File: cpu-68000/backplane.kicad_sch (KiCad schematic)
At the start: 12 parts, among them J201 Conn_03x32_Row_Letter_First

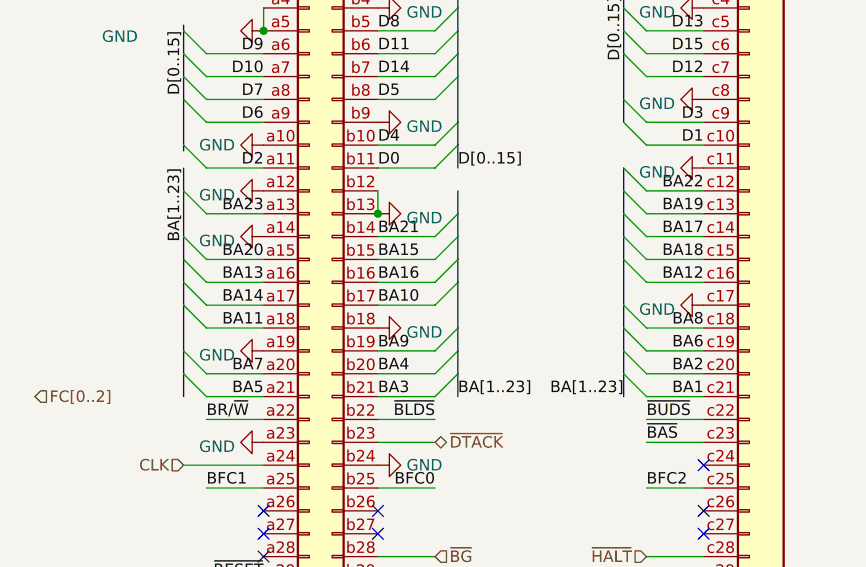
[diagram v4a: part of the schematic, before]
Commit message: Finished routing new address/data from backplane
- Routed the traces for the address/data bus from the connector and
  along the memories that need them. The NVRAM is fully connected to the
  bus, along with the peripheral section.

  We'll need to assign address lines to the SRAMs, then connect the
  flash chips next.
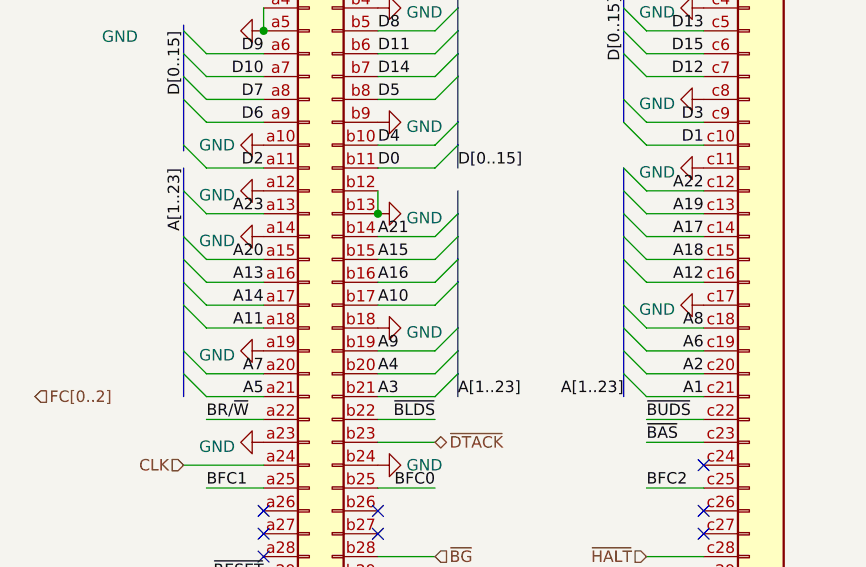
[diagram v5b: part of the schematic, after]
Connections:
- net A1: now also J201.c21 (Pin_c21)
- net A10: now also J201.b17 (Pin_b17)
- net A11: now also J201.a18 (Pin_a18)
- net A12: now also J201.c16 (Pin_c16)
- net A13: now also J201.a16 (Pin_a16)
- net A14: now also J201.a17 (Pin_a17)
- net A15: now also J201.b15 (Pin_b15)
- net A16: now also J201.b16 (Pin_b16)
- net A17: now also J201.c14 (Pin_c14)
- net A18: now also J201.c15 (Pin_c15)
- net A19: now also J201.c13 (Pin_c13)
- net A2: now also J201.c20 (Pin_c20)
- net A20: now also J201.a15 (Pin_a15)
- net A21: now also J201.b14 (Pin_b14)
- net A22: now also J201.c12 (Pin_c12)
- net A23: now also J201.a13 (Pin_a13)
- net A3: now also J201.b21 (Pin_b21)
- net A4: now also J201.b20 (Pin_b20)
- net A5: now also J201.a21 (Pin_a21)
- net A6: now also J201.c19 (Pin_c19)
- net A7: now also J201.a20 (Pin_a20)
- net A8: now also J201.c18 (Pin_c18)
- net A9: now also J201.b19 (Pin_b19)
- net BA1: no longer J201.c21 (Pin_c21)
- net BA10: no longer J201.b17 (Pin_b17)
- net BA11: no longer J201.a18 (Pin_a18)
- net BA12: no longer J201.c16 (Pin_c16)
- net BA13: no longer J201.a16 (Pin_a16)
- net BA14: no longer J201.a17 (Pin_a17)
- net BA15: no longer J201.b15 (Pin_b15)
- net BA16: no longer J201.b16 (Pin_b16)
- net BA17: no longer J201.c14 (Pin_c14)
- net BA18: no longer J201.c15 (Pin_c15)
- net BA19: no longer J201.c13 (Pin_c13)
- net BA2: no longer J201.c20 (Pin_c20)
- net BA20: no longer J201.a15 (Pin_a15)
- net BA21: no longer J201.b14 (Pin_b14)
- net BA22: no longer J201.c12 (Pin_c12)
- net BA23: no longer J201.a13 (Pin_a13)
- net BA3: no longer J201.b21 (Pin_b21)
- net BA4: no longer J201.b20 (Pin_b20)
- net BA5: no longer J201.a21 (Pin_a21)
- net BA6: no longer J201.c19 (Pin_c19)
- net BA7: no longer J201.a20 (Pin_a20)
- net BA8: no longer J201.c18 (Pin_c18)
- net BA9: no longer J201.b19 (Pin_b19)
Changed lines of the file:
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@@
     (effects (font (size 1.27 1.27)) (justify right bottom))
   )
-  (label "BA18" (at 264.16 54.61 180)
+  (label "A18" (at 264.16 54.61 180)
     (effects (font (size 1.27 1.27)) (justify right bottom))
   )
@@
     (effects (font (size 1.27 1.27)) (justify right bottom))
   )
-  (label "BA5" (at 215.265 69.85 180)
+  (label "A5" (at 215.265 69.85 180)
     (effects (font (size 1.27 1.27)) (justify right bottom))
   )
@@
     (effects (font (size 1.27 1.27)) (justify right bottom))
   )
-  (label "BA20" (at 215.265 54.61 180)
-    (effects (font (size 1.27 1.27)) (justify right bottom))
-  )
-  (label "BA2" (at 264.16 67.31 180)
-    (effects (font (size 1.27 1.27)) (justify right bottom))
-  )
-  (label "BA10" (at 227.965 59.69 0)
+  (label "A20" (at 215.265 54.61 180)
+    (effects (font (size 1.27 1.27)) (justify right bottom))
+  )
+  (label "A2" (at 264.16 67.31 180)
+    (effects (font (size 1.27 1.27)) (justify right bottom))
+  )
+  (label "A10" (at 227.965 59.69 0)
     (effects (font (size 1.27 1.27)) (justify left bottom))
   )
@@
     (effects (font (size 1.27 1.27)) (justify left bottom))
   )
-  (label "BA3" (at 227.965 69.85 0)
+  (label "A3" (at 227.965 69.85 0)
     (effects (font (size 1.27 1.27)) (justify left bottom))
   )
@@
     (effects (font (size 1.27 1.27)) (justify right bottom))
   )
-  (label "BA[1..23]" (at 255.27 69.85 180)
+  (label "A[1..23]" (at 255.27 69.85 180)
     (effects (font (size 1.27 1.27)) (justify right bottom))
   )
@@
     (effects (font (size 1.27 1.27)) (justify right bottom))
   )
-  (label "BA21" (at 227.965 52.07 0)
+  (label "A21" (at 227.965 52.07 0)
     (effects (font (size 1.27 1.27)) (justify left bottom))
   )
@@
     (effects (font (size 1.27 1.27)) (justify left bottom))
   )
-  (label "BA4" (at 227.965 67.31 0)
+  (label "A4" (at 227.965 67.31 0)
     (effects (font (size 1.27 1.27)) (justify left bottom))
   )
@@
     (effects (font (size 1.27 1.27)) (justify right bottom))
   )
-  (label "BA19" (at 264.16 49.53 180)
+  (label "A19" (at 264.16 49.53 180)
     (effects (font (size 1.27 1.27)) (justify right bottom))
   )
@@
     (effects (font (size 1.27 1.27)) (justify right bottom))
   )
-  (label "BA[1..23]" (at 236.855 69.85 0)
+  (label "A[1..23]" (at 236.855 69.85 0)
     (effects (font (size 1.27 1.27)) (justify left bottom))
   )
@@
     (effects (font (size 1.27 1.27)) (justify right bottom))
   )
-  (label "BA12" (at 264.16 57.15 180)
-    (effects (font (size 1.27 1.27)) (justify right bottom))
-  )
-  (label "BA14" (at 215.265 59.69 180)
+  (label "A12" (at 264.16 57.15 180)
+    (effects (font (size 1.27 1.27)) (justify right bottom))
+  )
+  (label "A14" (at 215.265 59.69 180)
     (effects (font (size 1.27 1.27)) (justify right bottom))
   )
@@
     (effects (font (size 1.27 1.27)) (justify right bottom))
   )
-  (label "BA7" (at 215.265 67.31 180)
+  (label "A7" (at 215.265 67.31 180)
     (effects (font (size 1.27 1.27)) (justify right bottom))
   )
@@
     (effects (font (size 1.27 1.27)) (justify left bottom))
   )
-  (label "BA11" (at 215.265 62.23 180)
+  (label "A11" (at 215.265 62.23 180)
     (effects (font (size 1.27 1.27)) (justify right bottom))
   )
@@
     (effects (font (size 1.27 1.27)) (justify left bottom))
   )
-  (label "BA17" (at 264.16 52.07 180)
+  (label "A17" (at 264.16 52.07 180)
     (effects (font (size 1.27 1.27)) (justify right bottom))
   )
@@
     (effects (font (size 1.27 1.27)) (justify left bottom))
   )
-  (label "BA15" (at 227.965 54.61 0)
+  (label "A15" (at 227.965 54.61 0)
     (effects (font (size 1.27 1.27)) (justify left bottom))
   )
@@
     (effects (font (size 1.27 1.27)) (justify right bottom))
   )
-  (label "BA8" (at 264.16 62.23 180)
+  (label "A8" (at 264.16 62.23 180)
     (effects (font (size 1.27 1.27)) (justify right bottom))
   )
@@
     (effects (font (size 1.27 1.27)) (justify right bottom))
   )
-  (label "BA23" (at 215.265 49.53 180)
+  (label "A23" (at 215.265 49.53 180)
     (effects (font (size 1.27 1.27)) (justify right bottom))
   )
@@
     (effects (font (size 1.27 1.27)) (justify right bottom))
   )
-  (label "BA22" (at 264.16 46.99 180)
+  (label "A22" (at 264.16 46.99 180)
     (effects (font (size 1.27 1.27)) (justify right bottom))
   )
@@
     (effects (font (size 1.27 1.27)) (justify left bottom))
   )
-  (label "BA1" (at 264.16 69.85 180)
-    (effects (font (size 1.27 1.27)) (justify right bottom))
-  )
-  (label "BA[1..23]" (at 206.375 44.45 270)
+  (label "A1" (at 264.16 69.85 180)
+    (effects (font (size 1.27 1.27)) (justify right bottom))
+  )
+  (label "A[1..23]" (at 206.375 44.45 270)
     (effects (font (size 1.27 1.27)) (justify right bottom))
   )
@@
     (effects (font (size 1.27 1.27)) (justify left bottom))
   )
-  (label "BA13" (at 215.265 57.15 180)
+  (label "A13" (at 215.265 57.15 180)
     (effects (font (size 1.27 1.27)) (justify right bottom))
   )
@@
     (effects (font (size 1.27 1.27)) (justify left bottom))
   )
-  (label "BA9" (at 227.965 64.77 0)
-    (effects (font (size 1.27 1.27)) (justify left bottom))
-  )
-  (label "BA6" (at 264.16 64.77 180)
+  (label "A9" (at 227.965 64.77 0)
+    (effects (font (size 1.27 1.27)) (justify left bottom))
+  )
+  (label "A6" (at 264.16 64.77 180)
     (effects (font (size 1.27 1.27)) (justify right bottom))
   )
@@
     (effects (font (size 1.27 1.27)) (justify right bottom))
   )
-  (label "BA16" (at 227.965 57.15 0)
-    (effects (font (size 1.27 1.27)) (justify left bottom))
-  )
+  (label "A16" (at 227.965 57.15 0)
+    (effects (font (size 1.27 1.27)) (justify left bottom))
+  )

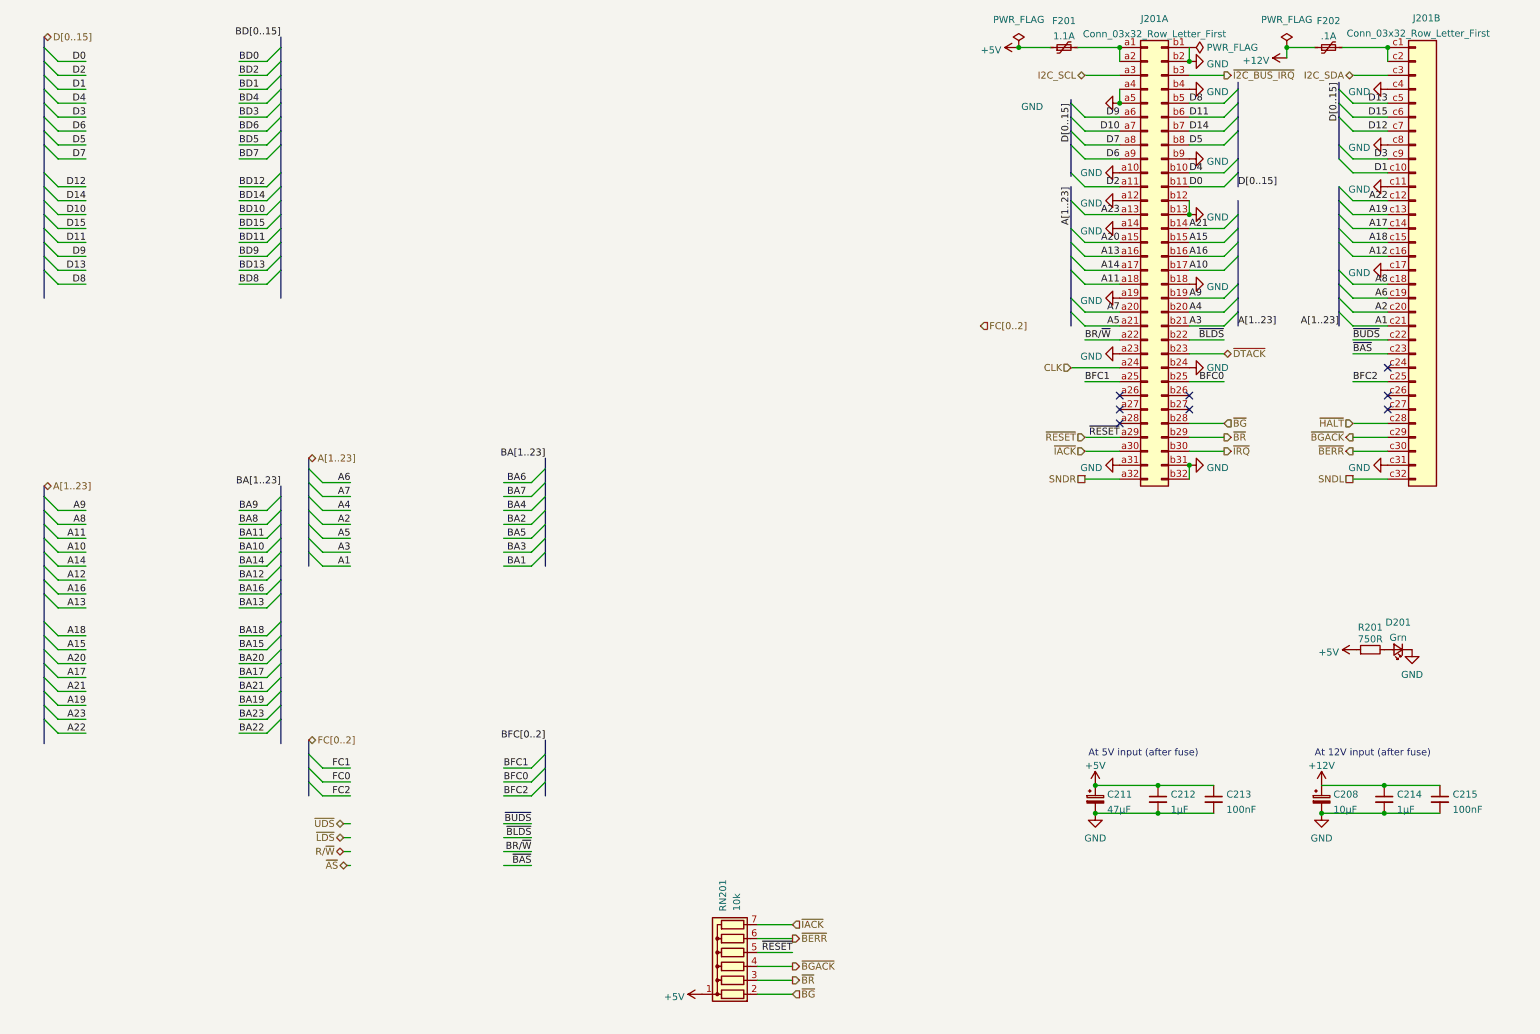
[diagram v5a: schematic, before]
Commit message: Finished rework of CPU card
- All the busses are finished routing. The board is feature wise
  identical to rev 1, sans buffers, and with DIP boot ROM sockets rather
  than soldered flash.

- Corrected a few remaining bugs on the board, namely the incorrect
  footprint for the +12V fuse.
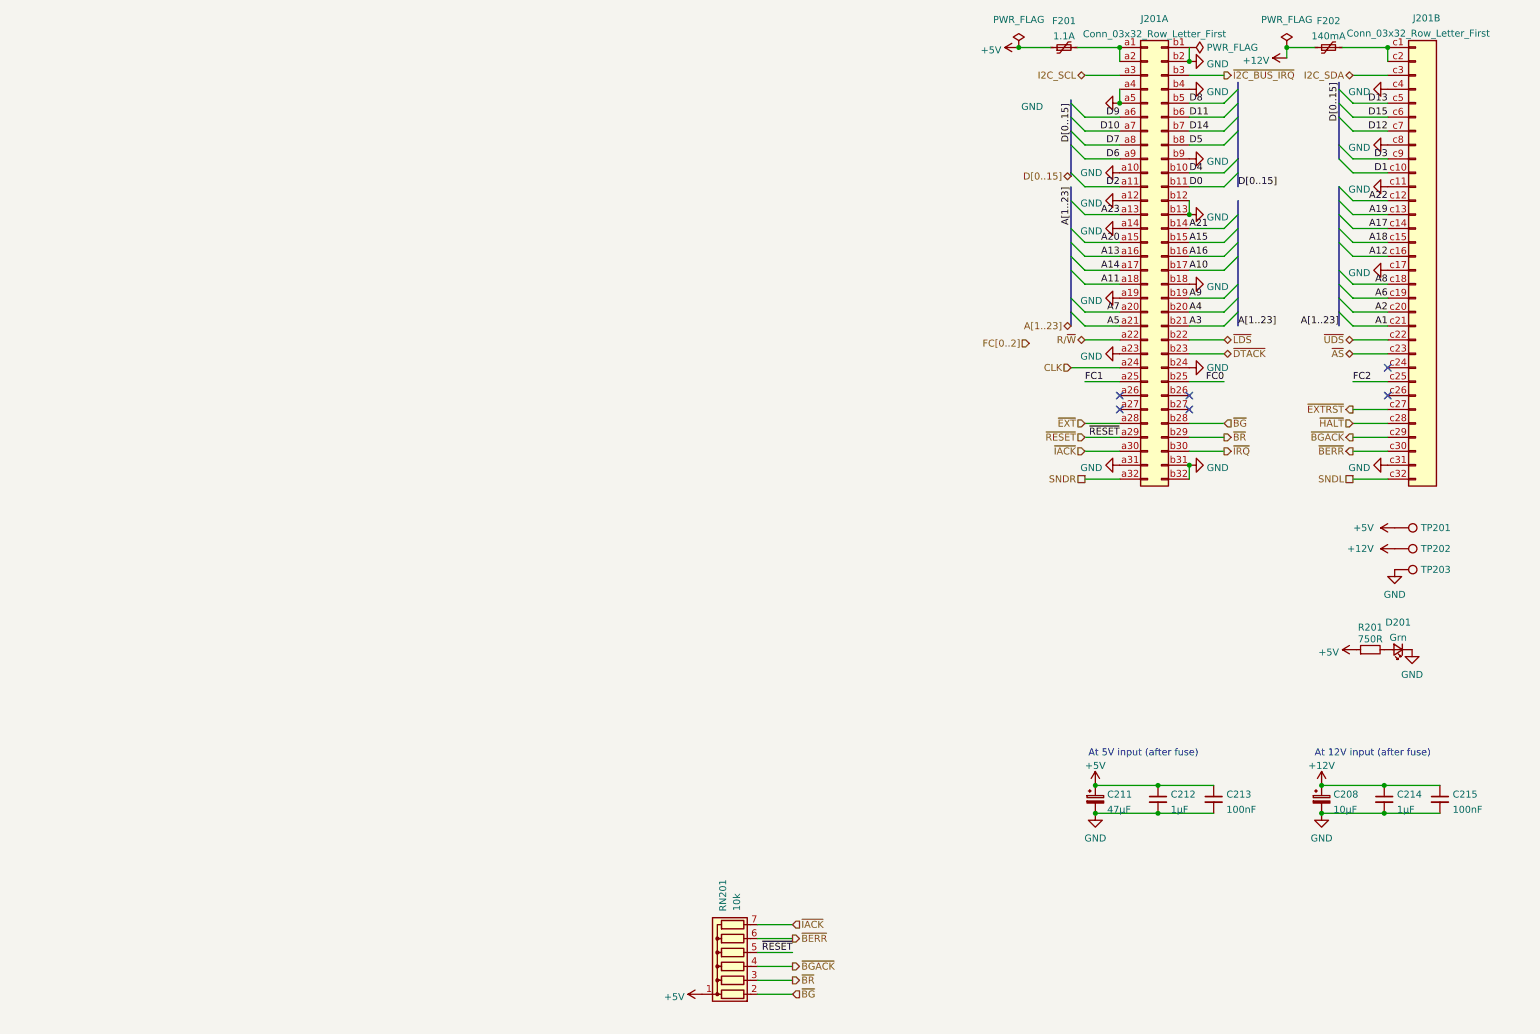
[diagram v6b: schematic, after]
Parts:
- added TP201: +5V, TestPoint:TestPoint_Loop_D2.60mm_Drill1.4mm_Beaded, symbol Connector:TestPoint
- added TP202: +12V, TestPoint:TestPoint_Loop_D2.60mm_Drill1.4mm_Beaded, symbol Connector:TestPoint
- added TP203: GND, TestPoint:TestPoint_Loop_D2.60mm_Drill1.4mm_Beaded, symbol Connector:TestPoint
- F202: value .1A -> 140mA; footprint Fuse:Fuse_Littelfuse-NANO2-451_453 -> Fuse:Fuse_1812_4532Metric; MPN NANOSMDC010F-2 -> 0ZCG0014FF2C
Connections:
- net BFC0 is gone; now on net FC0: J201.b25 (Pin_b25)
- net BFC1 is gone; now on net FC1: J201.a25 (Pin_a25)
- net BFC2 is gone; now on net FC2: J201.c25 (Pin_c25)
- net BR/~{W} is gone; now on net R/~{W}: J201.a22 (Pin_a22)
- net ~{BAS} is gone; now on net ~{AS}: J201.c23 (Pin_c23)
- net ~{BLDS} is gone; now on net ~{LDS}: J201.b22 (Pin_b22)
- net ~{BUDS} is gone; now on net ~{UDS}: J201.c22 (Pin_c22)
- net +12V: now also TP202.1
- net +5V: now also TP201.1
- net GND: now also TP203.1
- net ~{EXTRST}: now reaches J201.c27 (Pin_c27)
- net ~{EXT}: now reaches J201.a28 (Pin_a28)
- no-connect marks 8 -> 6

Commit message: Minor tweaks to all boards
- Moved around some traces on the 68000 CPU card for prettiness

- Added a connector on the backplane to provide +5V/+12V without a
  management card installed (for testing)
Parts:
- D201: MPN H100CGD -> H101CGD
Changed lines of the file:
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@@
   (title_block
     (title "68komputer CPU Board")
-    (date "2021-12-30")
+    (date "2022-01-09")
     (rev "2")
     (company "Tristan Seifert")
@@
       (effects (font (size 1.27 1.27)) hide)
     )
-    (property "MPN" "H100CGD" (id 4) (at 266.065 128.905 0)
-      (effects (font (size 1.27 1.27)) hide)
-    )
+    (property "MPN" "H101CGD" (id 4) (at 266.065 128.905 0)
+      (effects (font (size 1.27 1.27)) hide)
+    )

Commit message: Minor layout tweaks across the board
- Added an input for a test clock, and a jumper for sending this clock
  instead of the CPU clock to the clock pins of the expansion cards on
  the backplane boards

- Reworked a bunch of the power supply board

- Minor changes (to consolidate BOMs) on CPU board for some capacitors,
  they were replaced with SMD versions
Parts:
- C211: footprint Capacitor_THT:CP_Radial_D6.3mm_P2.50mm -> Capacitor_SMD:CP_Elec_6.3x5.7; MPN A750EK476M1EAAE040 -> A768EB476M1VLAS042
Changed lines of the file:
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@@
       (effects (font (size 1.27 1.27)) (justify left))
     )
-    (property "Footprint" "Capacitor_THT:CP_Radial_D6.3mm_P2.50mm" (id 2) (at 210.82 156.21 0)
+    (property "Footprint" "Capacitor_SMD:CP_Elec_6.3x5.7" (id 2) (at 210.82 156.21 0)
       (effects (font (size 1.27 1.27)) hide)
     )
@@
       (effects (font (size 1.27 1.27)) hide)
     )
-    (property "MPN" "A750EK476M1EAAE040" (id 4) (at 210.82 156.21 0)
+    (property "MPN" "A768EB476M1VLAS042" (id 4) (at 210.82 156.21 0)
       (effects (font (size 1.27 1.27)) hide)
     )
